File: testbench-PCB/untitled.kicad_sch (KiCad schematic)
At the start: 5 parts, among them J1 USB_C_Receptacle_USB2.0

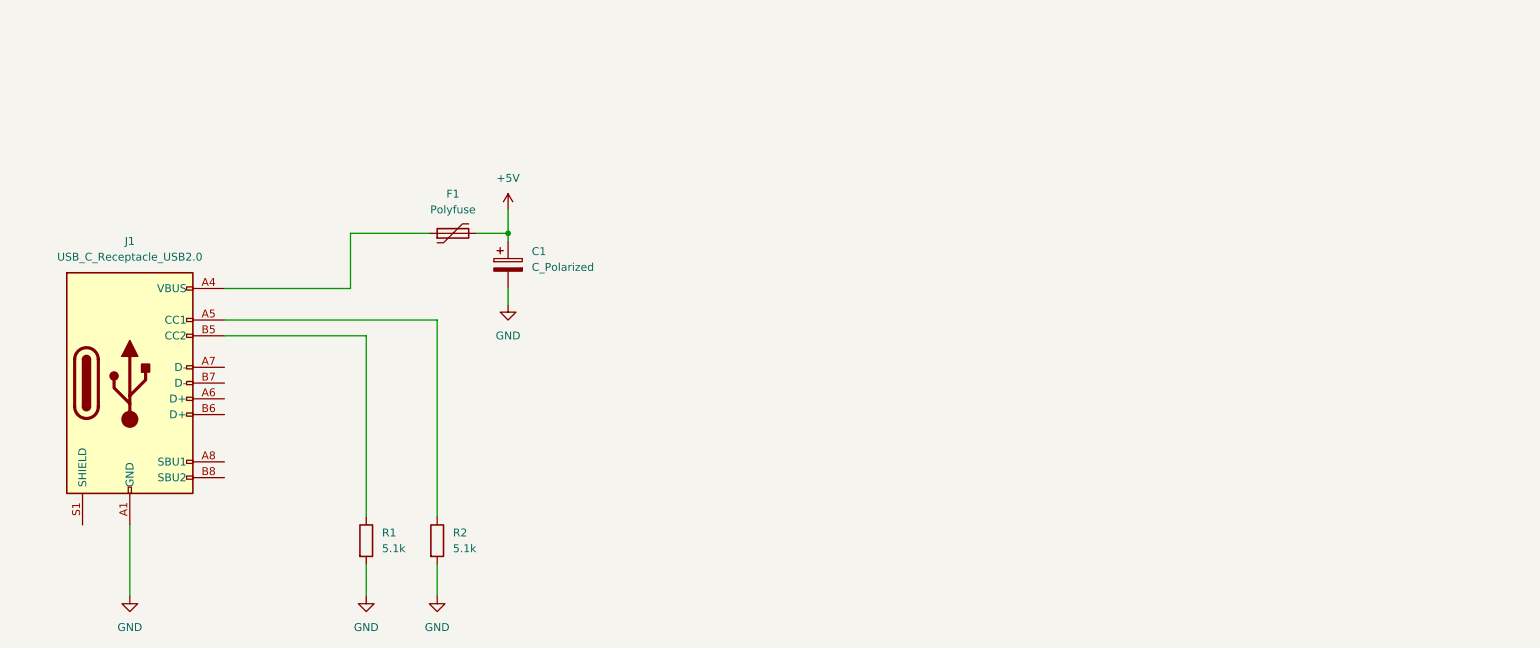
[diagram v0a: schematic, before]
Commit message: Added connection between some modules.
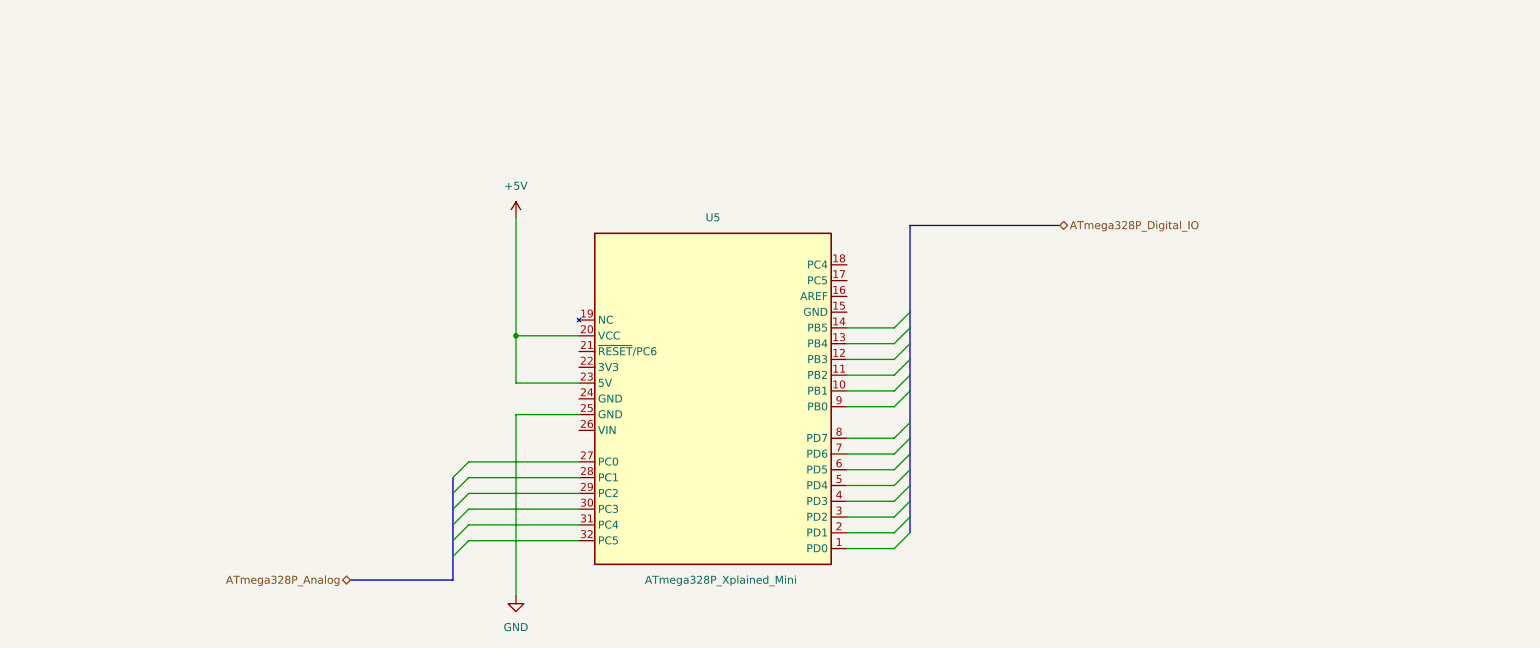
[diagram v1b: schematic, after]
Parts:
- removed C1: C_Polarized, symbol Device:C_Polarized
- removed F1: Polyfuse, symbol Device:Polyfuse
- removed J1: USB_C_Receptacle_USB2.0, symbol Connector:USB_C_Receptacle_USB2.0
- removed R1, R2: 5.1k, symbol Device:R
- added U5: ATmega328P_Xplained_Mini, kit_modules:ATmega328P_Xplained_Mini, symbol kit_modules:ATmega328P_Xplained_mini
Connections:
- net +5V: now also U5.20 (VCC), U5.23 (5V)
- net GND: now also U5.25 (GND)

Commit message: Finished connection between modules and MCU.
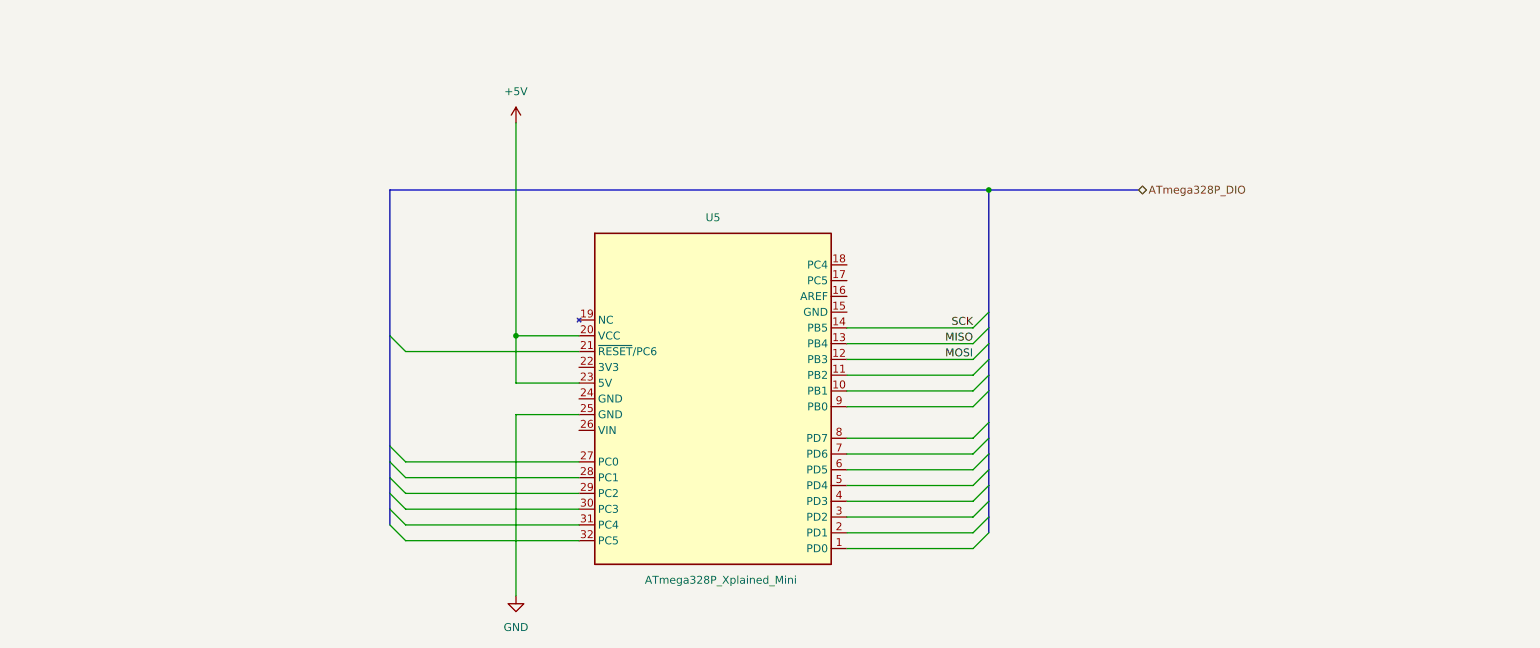
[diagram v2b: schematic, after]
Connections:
- net MOSI: now reaches U5.12 (PB3)
- net MISO: now reaches U5.13 (PB4)
- net SCK: now reaches U5.14 (PB5)

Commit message: Changed naming convention.
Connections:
- net GND: now also U5.15 (GND)
- no-connect marks 0 -> 6
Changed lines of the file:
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@@
   (junction (at 109.22 73.66) (diameter 0) (color 0 0 0 0)
   )
-  (junction (at 185.42 50.165) (diameter 0) (color 0 0 0 0)
-  )
+  (no_connect (at 162.56 62.23))
+  (no_connect (at 119.38 78.74))
+  (no_connect (at 119.38 88.9))
+  (no_connect (at 162.56 67.31))
+  (no_connect (at 162.56 64.77))
+  (no_connect (at 119.38 83.82))
   (bus_entry (at 88.9 104.14) (size 2.54 2.54)
     (stroke (width 0) (type default))
@@
     (stroke (width 0) (type default))
   )
-  (bus (pts (xy 185.42 50.165) (xy 209.55 50.165))
+  (bus (pts (xy 185.42 72.39) (xy 185.42 74.93))
+    (stroke (width 0) (type default))
+  )
+  (bus (pts (xy 88.9 50.165) (xy 209.55 50.165))
+    (stroke (width 0) (type default))
+  )
+  (bus (pts (xy 185.42 90.17) (xy 185.42 92.71))
     (stroke (width 0) (type default))
   )
@@
     (stroke (width 0) (type default))
   )
+  (bus (pts (xy 185.42 102.87) (xy 185.42 105.41))
+    (stroke (width 0) (type default))
+  )
   (bus (pts (xy 88.9 99.06) (xy 88.9 96.52))
     (stroke (width 0) (type default))
   )
+  (bus (pts (xy 185.42 95.25) (xy 185.42 97.79))
+    (stroke (width 0) (type default))
+  )
   (wire (pts (xy 91.44 76.2) (xy 119.38 76.2))
     (stroke (width 0) (type default))
   )
+  (bus (pts (xy 185.42 80.01) (xy 185.42 82.55))
+    (stroke (width 0) (type default))
+  )
+  (bus (pts (xy 185.42 69.85) (xy 185.42 72.39))
+    (stroke (width 0) (type default))
+  )
   (wire (pts (xy 162.56 80.01) (xy 182.88 80.01))
     (stroke (width 0) (type default))
   )
+  (wire (pts (xy 168.91 113.03) (xy 168.91 69.85))
+    (stroke (width 0) (type default))
+  )
   (wire (pts (xy 162.56 74.93) (xy 182.88 74.93))
     (stroke (width 0) (type default))
@@
     (stroke (width 0) (type default))
   )
-  (bus (pts (xy 88.9 50.165) (xy 185.42 50.165))
-    (stroke (width 0) (type default))
-  )
-  (bus (pts (xy 185.42 105.41) (xy 185.42 102.87))
-    (stroke (width 0) (type default))
-  )
   (wire (pts (xy 109.22 73.66) (xy 109.22 39.37))
     (stroke (width 0) (type default))
   )
-  (bus (pts (xy 185.42 102.87) (xy 185.42 100.33))
-    (stroke (width 0) (type default))
-  )
-  (bus (pts (xy 185.42 77.47) (xy 185.42 74.93))
-    (stroke (width 0) (type default))
-  )
   (wire (pts (xy 162.56 90.17) (xy 182.88 90.17))
     (stroke (width 0) (type default))
@@
     (stroke (width 0) (type default))
   )
+  (bus (pts (xy 185.42 100.33) (xy 185.42 102.87))
+    (stroke (width 0) (type default))
+  )
   (wire (pts (xy 91.44 93.98) (xy 119.38 93.98))
     (stroke (width 0) (type default))
@@
     (stroke (width 0) (type default))
   )
-  (bus (pts (xy 185.42 69.85) (xy 185.42 50.165))
+  (wire (pts (xy 168.91 69.85) (xy 162.56 69.85))
     (stroke (width 0) (type default))
   )
@@
     (stroke (width 0) (type default))
   )
-  (bus (pts (xy 185.42 82.55) (xy 185.42 80.01))
-    (stroke (width 0) (type default))
-  )
-  (bus (pts (xy 185.42 87.63) (xy 185.42 82.55))
-    (stroke (width 0) (type default))
-  )
   (wire (pts (xy 91.44 106.68) (xy 119.38 106.68))
     (stroke (width 0) (type default))
@@
     (stroke (width 0) (type default))
   )
+  (bus (pts (xy 185.42 50.8) (xy 185.42 69.85))
+    (stroke (width 0) (type default))
+  )
   (bus (pts (xy 88.9 101.6) (xy 88.9 99.06))
     (stroke (width 0) (type default))
@@
     (stroke (width 0) (type default))
   )
-  (bus (pts (xy 185.42 72.39) (xy 185.42 69.85))
-    (stroke (width 0) (type default))
-  )
-  (bus (pts (xy 185.42 74.93) (xy 185.42 72.39))
+  (bus (pts (xy 185.42 74.93) (xy 185.42 77.47))
     (stroke (width 0) (type default))
   )
@@
     (stroke (width 0) (type default))
   )
-  (bus (pts (xy 185.42 95.25) (xy 185.42 92.71))
+  (bus (pts (xy 185.42 77.47) (xy 185.42 80.01))
+    (stroke (width 0) (type default))
+  )
+  (bus (pts (xy 185.42 87.63) (xy 185.42 90.17))
     (stroke (width 0) (type default))
   )
@@
     (stroke (width 0) (type default))
   )
-  (bus (pts (xy 185.42 80.01) (xy 185.42 77.47))
-    (stroke (width 0) (type default))
-  )
-  (bus (pts (xy 185.42 92.71) (xy 185.42 90.17))
+  (bus (pts (xy 185.42 92.71) (xy 185.42 95.25))
+    (stroke (width 0) (type default))
+  )
+  (bus (pts (xy 185.42 97.79) (xy 185.42 100.33))
+    (stroke (width 0) (type default))
+  )
+  (bus (pts (xy 185.42 82.55) (xy 185.42 87.63))
     (stroke (width 0) (type default))
   )
@@
     (stroke (width 0) (type default))
   )
-  (bus (pts (xy 185.42 100.33) (xy 185.42 97.79))
-    (stroke (width 0) (type default))
-  )
   (wire (pts (xy 119.38 81.28) (xy 109.22 81.28))
     (stroke (width 0) (type default))
   )
   (wire (pts (xy 109.22 73.66) (xy 119.38 73.66))
-    (stroke (width 0) (type default))
-  )
-  (bus (pts (xy 185.42 97.79) (xy 185.42 95.25))
-    (stroke (width 0) (type default))
-  )
-  (bus (pts (xy 185.42 90.17) (xy 185.42 87.63))
     (stroke (width 0) (type default))
   )
@@
     (effects (font (size 1.27 1.27)) (justify right bottom))
   )
-  (hierarchical_label "ATmega328P_DIO" (shape bidirectional) (at 209.55 50.165 0) (fields_autoplaced)
+  (hierarchical_label "DUT[0..20]" (shape bidirectional) (at 209.55 50.165 0) (fields_autoplaced)
     (effects (font (size 1.27 1.27)) (justify left))
   )
@@
         )
       )
+    )
+  )
+  (symbol (lib_id "power:GND") (at 168.91 113.03 0) (unit 1)
+    (in_bom yes) (on_board yes) (dnp no) (fields_autoplaced)
+    (property "Reference" "#PWR040" (at 168.91 119.38 0)
+      (effects (font (size 1.27 1.27)) hide)
+    )
+    (property "Value" "GND" (at 168.91 118.11 0)
+      (effects (font (size 1.27 1.27)))
+    )
+    (property "Footprint" "" (at 168.91 113.03 0)
+      (effects (font (size 1.27 1.27)) hide)
+    )
+    (property "Datasheet" "" (at 168.91 113.03 0)
+      (effects (font (size 1.27 1.27)) hide)
+    )
+    (pin "1")
+    (instances
+      (project "testbench"
+        (path "/3ac6901d-218d-4b34-8c4a-bf7c417c33bc/6e28d1d5-7dc0-46ee-b3e4-ac6f56efc8b0"
+          (reference "#PWR040") (unit 1)
+        )
+      )

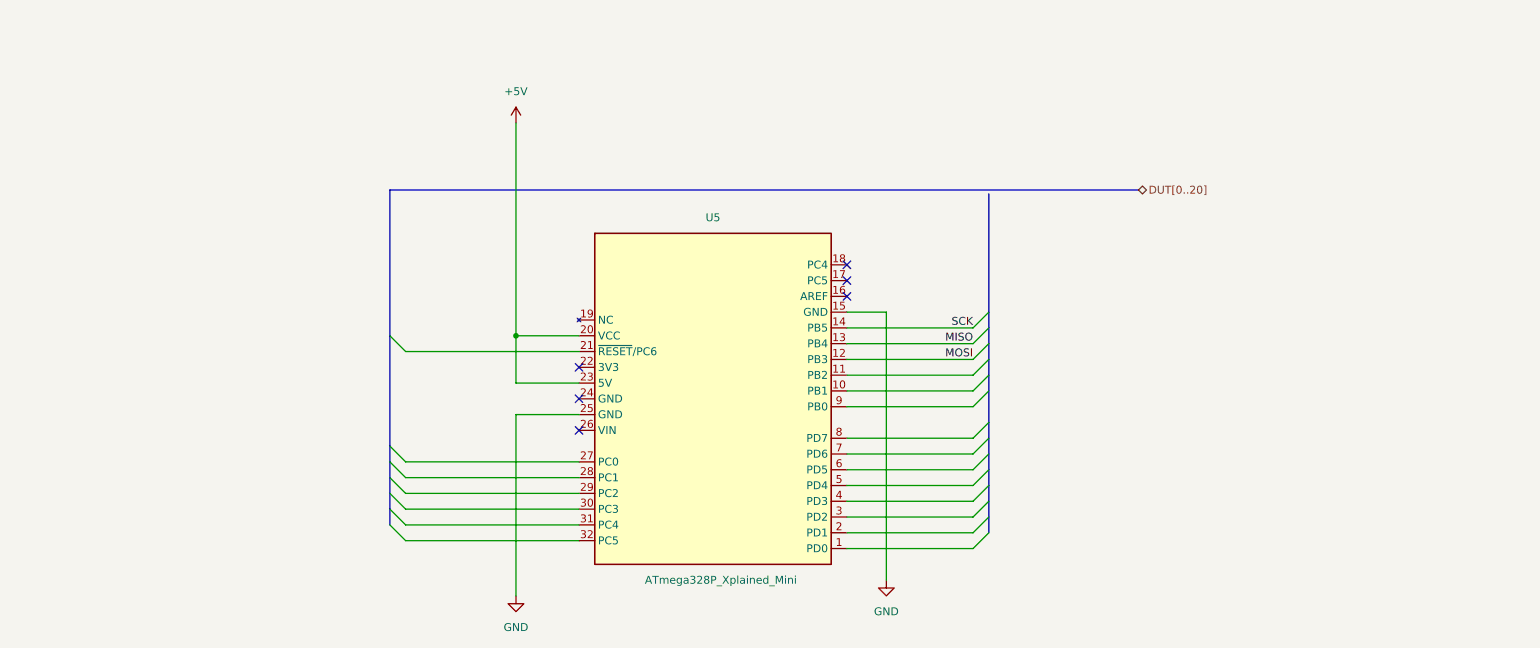
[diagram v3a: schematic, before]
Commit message: Rearanged PCB, updated footprints.
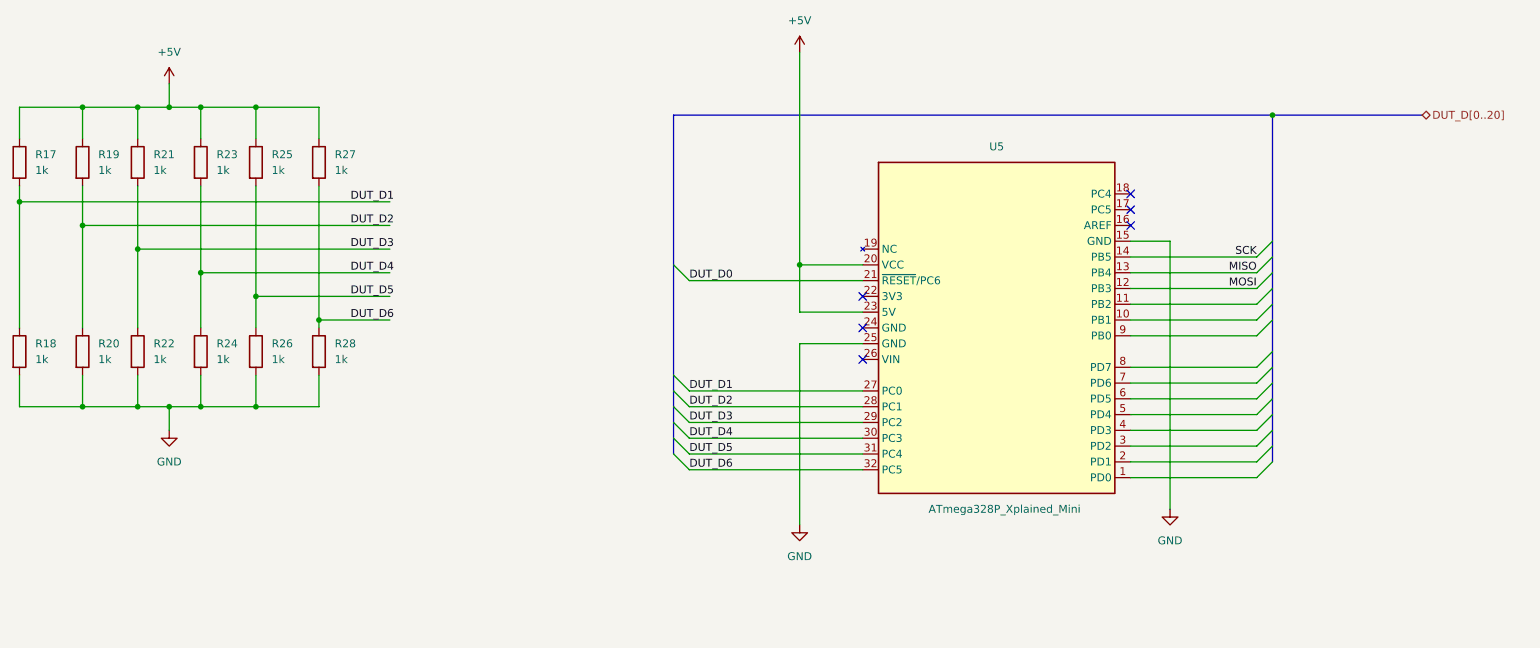
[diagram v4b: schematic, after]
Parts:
- added R17, R18, R19, R20, R21, R22, R23, R24, R25, R26, R27, R28: 1k, symbol Device:R
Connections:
- net +5V: now also R17.1, R19.1, R21.1, R23.1, R25.1, R27.1
- net GND: now also R18.2, R20.2, R22.2, R24.2, R26.2, R28.2
- net DUT_D0: now reaches U5.21 (~{RESET}/PC6)
- net DUT_D1: now reaches U5.27 (PC0)
- net DUT_D1: now also R17.2, R18.1
- net DUT_D2: now reaches U5.28 (PC1)
- net DUT_D2: now also R19.2, R20.1
- net DUT_D3: now reaches U5.29 (PC2)
- net DUT_D3: now also R21.2, R22.1
- net DUT_D4: now reaches U5.30 (PC3)
- net DUT_D4: now also R23.2, R24.1
- net DUT_D5: now reaches U5.31 (PC4)
- net DUT_D5: now also R25.2, R26.1
- net DUT_D6: now reaches U5.32 (PC5)
- net DUT_D6: now also R27.2, R28.1
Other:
- moved on the sheet: U5
